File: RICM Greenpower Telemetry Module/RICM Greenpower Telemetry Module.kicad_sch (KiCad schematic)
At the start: 56 parts, among them J1 Jack-DC, J10 Conn_01x02_Female, J11 Conn_01x02_Female, J2 Conn_01x04_Female, J3 Conn_01x05_Female, J4 Conn_01x03_Female, J5 Conn_01x03_Female, J6 Conn_01x02_Female, J7 Conn_01x02_Female, J8 Conn_01x02_Female, J9 Conn_01x04_Female, U1 XL2001E1, U2 MT92165, U3 Pico, U4 Adafruit_MicroSD_SPI_SDIO, U5 ADS7830, U6 MPU_6050_module

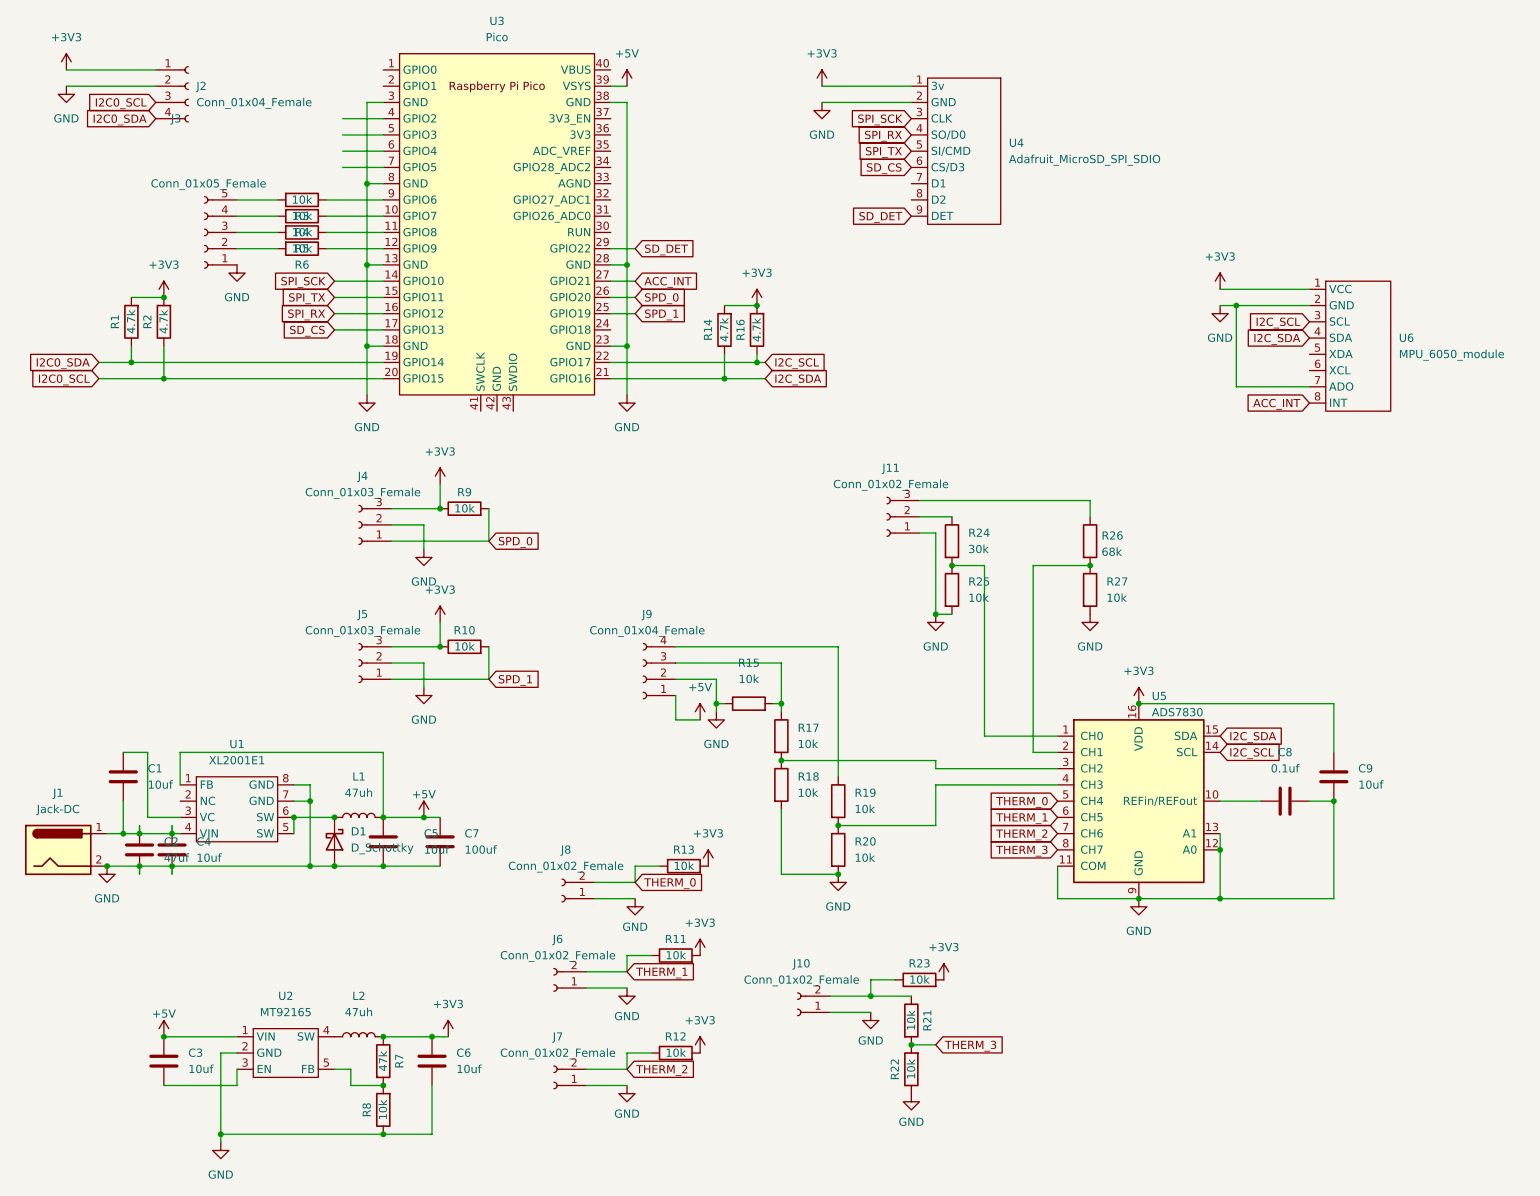
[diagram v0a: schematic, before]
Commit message: fixed errors discovered in v1 board
Connected vref on the ADS7830 to 3v3.
Corrected swapped pins on MT9216.
Added silkscreens and readjusted connector numbering.
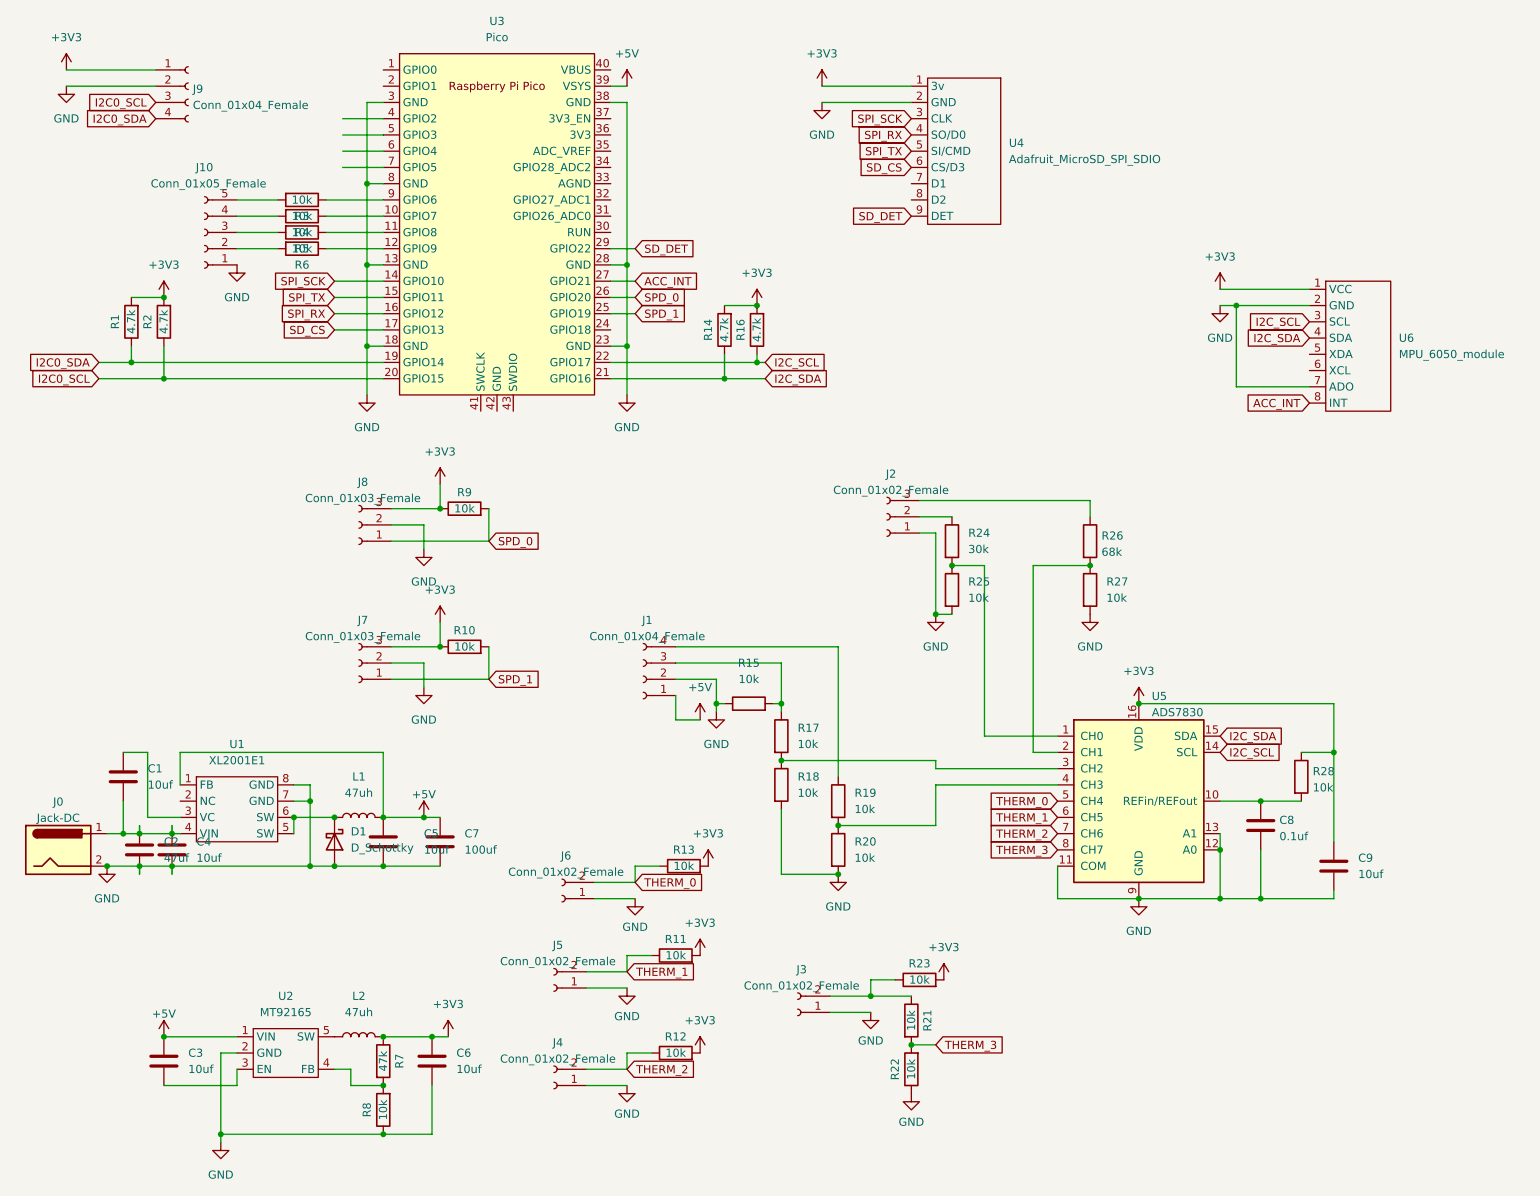
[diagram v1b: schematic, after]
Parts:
- added R28: 10k, Resistor_SMD:R_1206_3216Metric, symbol Device:R
- renumbered J1 to J0, J9 to J1, J3 to J10, J11 to J2, J10 to J3, J7 to J4, J6 to J5, J8 to J6, J5 to J7, J4 to J8, J2 to J9
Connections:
- net +3V3: now also R28.1
- net GND: now also C8.1; no longer C8.2
- net at R7.2, R8.2: now also U2.4 (FB); no longer U2.5 (FB)
- net at U5.10 (REFin/REFout): now also C8.2, R28.2; no longer C8.1
- net at L2.1: now also U2.5 (SW); no longer U2.4 (SW)
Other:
- moved on the sheet: C8, C9

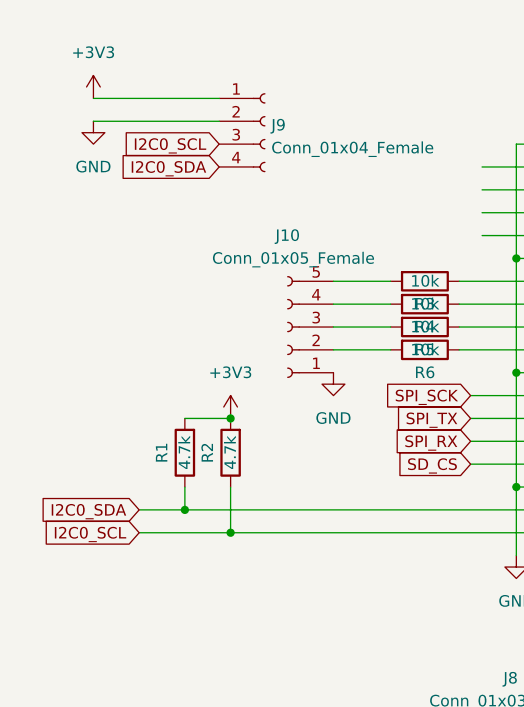
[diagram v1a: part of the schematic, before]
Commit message: added diags, bugfixes
Added libraries and associated diagnostics for OLED screens and GPIO buttons.
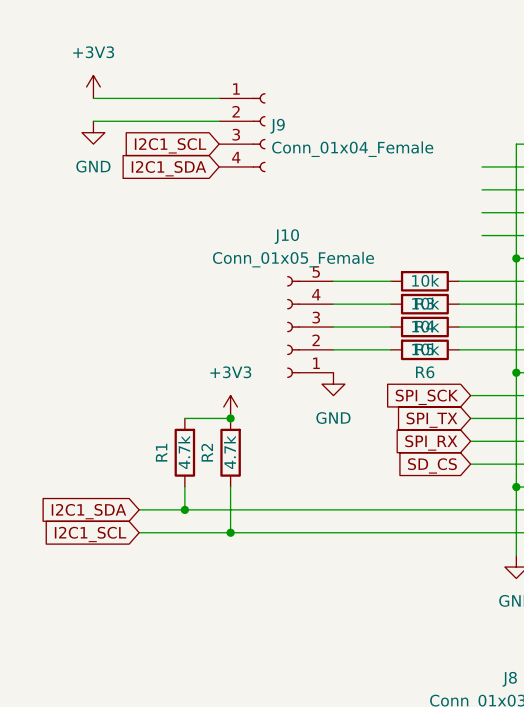
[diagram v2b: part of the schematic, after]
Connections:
- net I2C0_SCL renamed I2C1_SCL
- net I2C0_SDA renamed I2C1_SDA
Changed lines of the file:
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@@
     )
   )
-  (global_label "I2C0_SDA" (shape input) (at 34.29 30.48 180) (fields_autoplaced)
+  (global_label "I2C1_SDA" (shape input) (at 34.29 30.48 180) (fields_autoplaced)
     (effects (font (size 1.27 1.27)) (justify right))
-    (property "Intersheet References" "${INTERSHEET_REFS}" (id 0) (at 23.0474 30.5594 0)
+    (property "Intersheet References" "${INTERSHEET_REFS}" (id 0) (at 23.0474 30.4006 0)
       (effects (font (size 1.27 1.27)) (justify right) hide)
     )
@@
     )
   )
-  (global_label "I2C0_SCL" (shape input) (at 25.4 71.12 180) (fields_autoplaced)
+  (global_label "I2C1_SCL" (shape input) (at 25.4 71.12 180) (fields_autoplaced)
     (effects (font (size 1.27 1.27)) (justify right))
-    (property "Intersheet References" "${INTERSHEET_REFS}" (id 0) (at 14.2179 71.1994 0)
+    (property "Intersheet References" "${INTERSHEET_REFS}" (id 0) (at 14.2179 71.0406 0)
       (effects (font (size 1.27 1.27)) (justify right) hide)
     )
@@
     )
   )
-  (global_label "I2C0_SCL" (shape input) (at 34.29 27.94 180) (fields_autoplaced)
+  (global_label "I2C1_SCL" (shape input) (at 34.29 27.94 180) (fields_autoplaced)
     (effects (font (size 1.27 1.27)) (justify right))
-    (property "Intersheet References" "${INTERSHEET_REFS}" (id 0) (at 23.1079 28.0194 0)
+    (property "Intersheet References" "${INTERSHEET_REFS}" (id 0) (at 23.1079 27.8606 0)
       (effects (font (size 1.27 1.27)) (justify right) hide)
     )
@@
     )
   )
-  (global_label "I2C0_SDA" (shape input) (at 25.4 68.58 180) (fields_autoplaced)
+  (global_label "I2C1_SDA" (shape input) (at 25.4 68.58 180) (fields_autoplaced)
     (effects (font (size 1.27 1.27)) (justify right))
-    (property "Intersheet References" "${INTERSHEET_REFS}" (id 0) (at 14.1574 68.6594 0)
+    (property "Intersheet References" "${INTERSHEET_REFS}" (id 0) (at 14.1574 68.5006 0)
       (effects (font (size 1.27 1.27)) (justify right) hide)
     )

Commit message: Fixed footprints and silkscreen
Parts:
- C2: footprint Capacitor_THT:CP_Radial_D8.0mm_P3.50mm -> Capacitor_THT:CP_Radial_D5.0mm_P2.00mm
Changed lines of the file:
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@@
       (effects (font (size 1.27 1.27)) (justify left))
     )
-    (property "Footprint" "Capacitor_THT:CP_Radial_D8.0mm_P3.50mm" (id 2) (at 32.7152 148.59 0)
+    (property "Footprint" "Capacitor_THT:CP_Radial_D5.0mm_P2.00mm" (id 2) (at 32.7152 148.59 0)
       (effects (font (size 1.27 1.27)) hide)
     )
@@
     )
     (path "/0d18f623-67ed-4824-a618-f2eb436b25c6"
-      (reference "C2") (unit 1) (value "47uf") (footprint "Capacitor_THT:CP_Radial_D8.0mm_P3.50mm")
+      (reference "C2") (unit 1) (value "47uf") (footprint "Capacitor_THT:CP_Radial_D5.0mm_P2.00mm")
     )
     (path "/71b5cd3e-ae0b-4068-9f4c-5ceaa9425277"

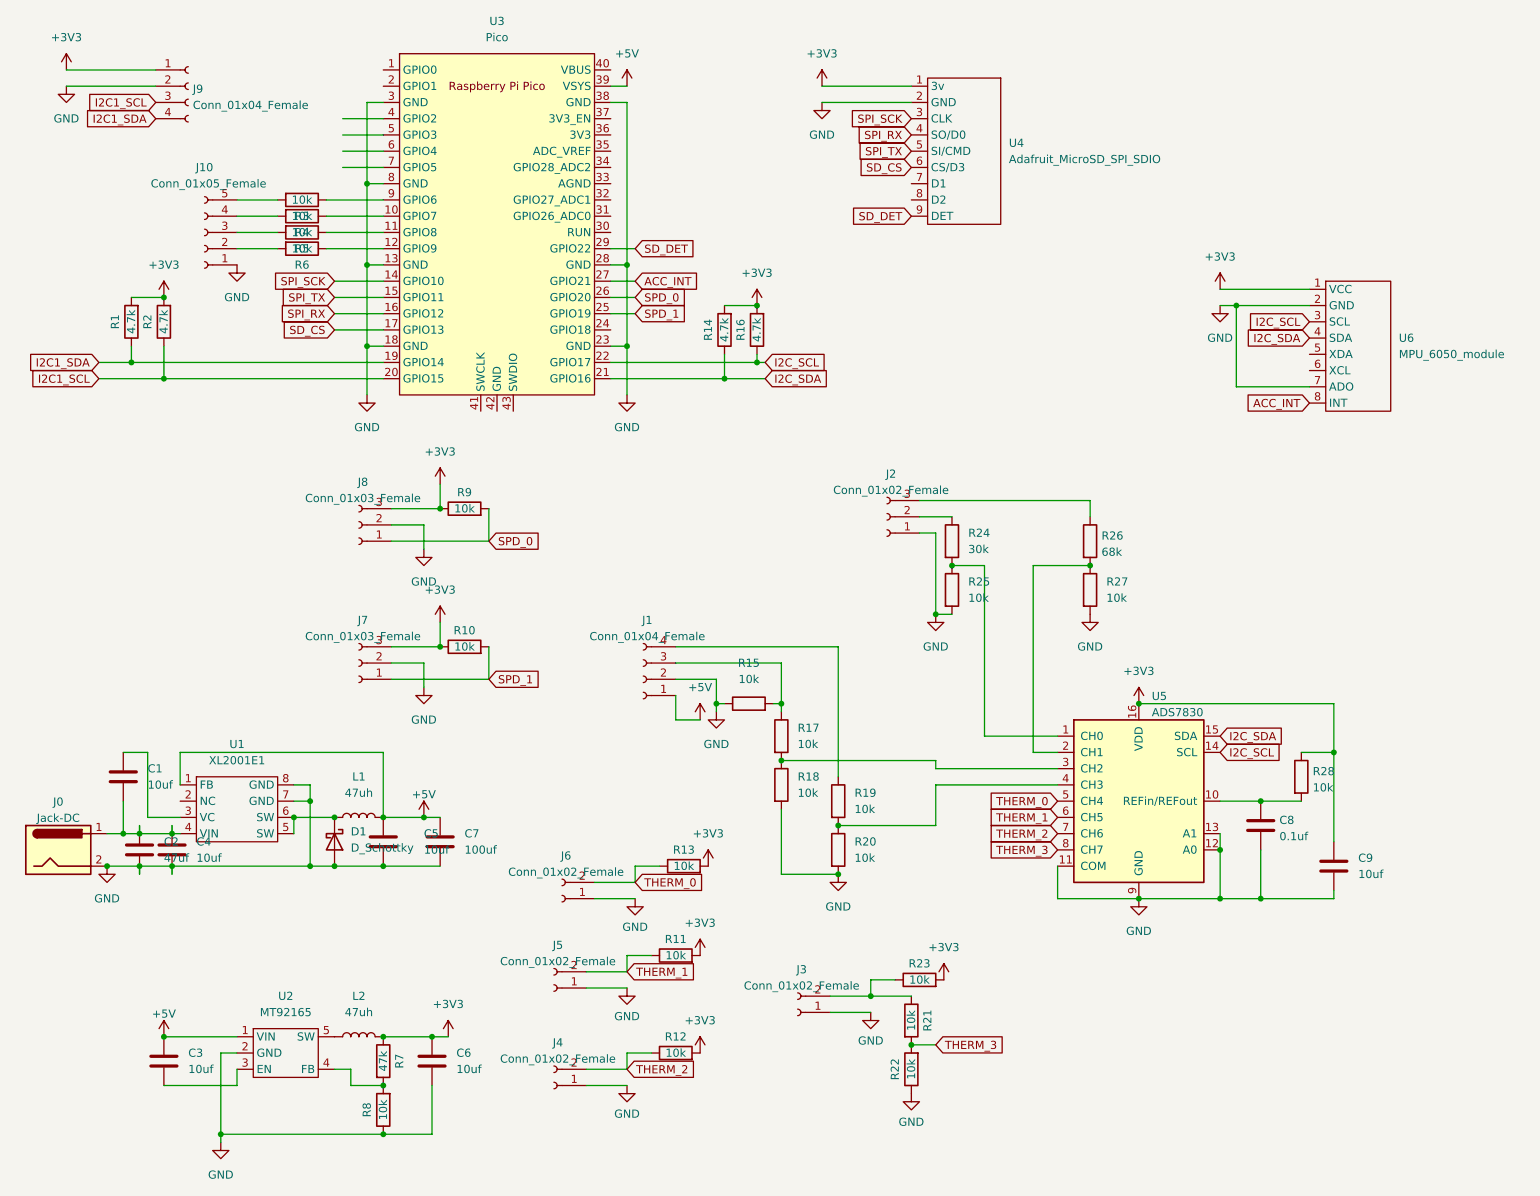
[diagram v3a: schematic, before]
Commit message: Schematic and layout corrections
Added revision silkscreen to schematic. Fixed pinout of display connector to match standard i2c pinout. Added schematic notes explaining resistor options for THERM_3.
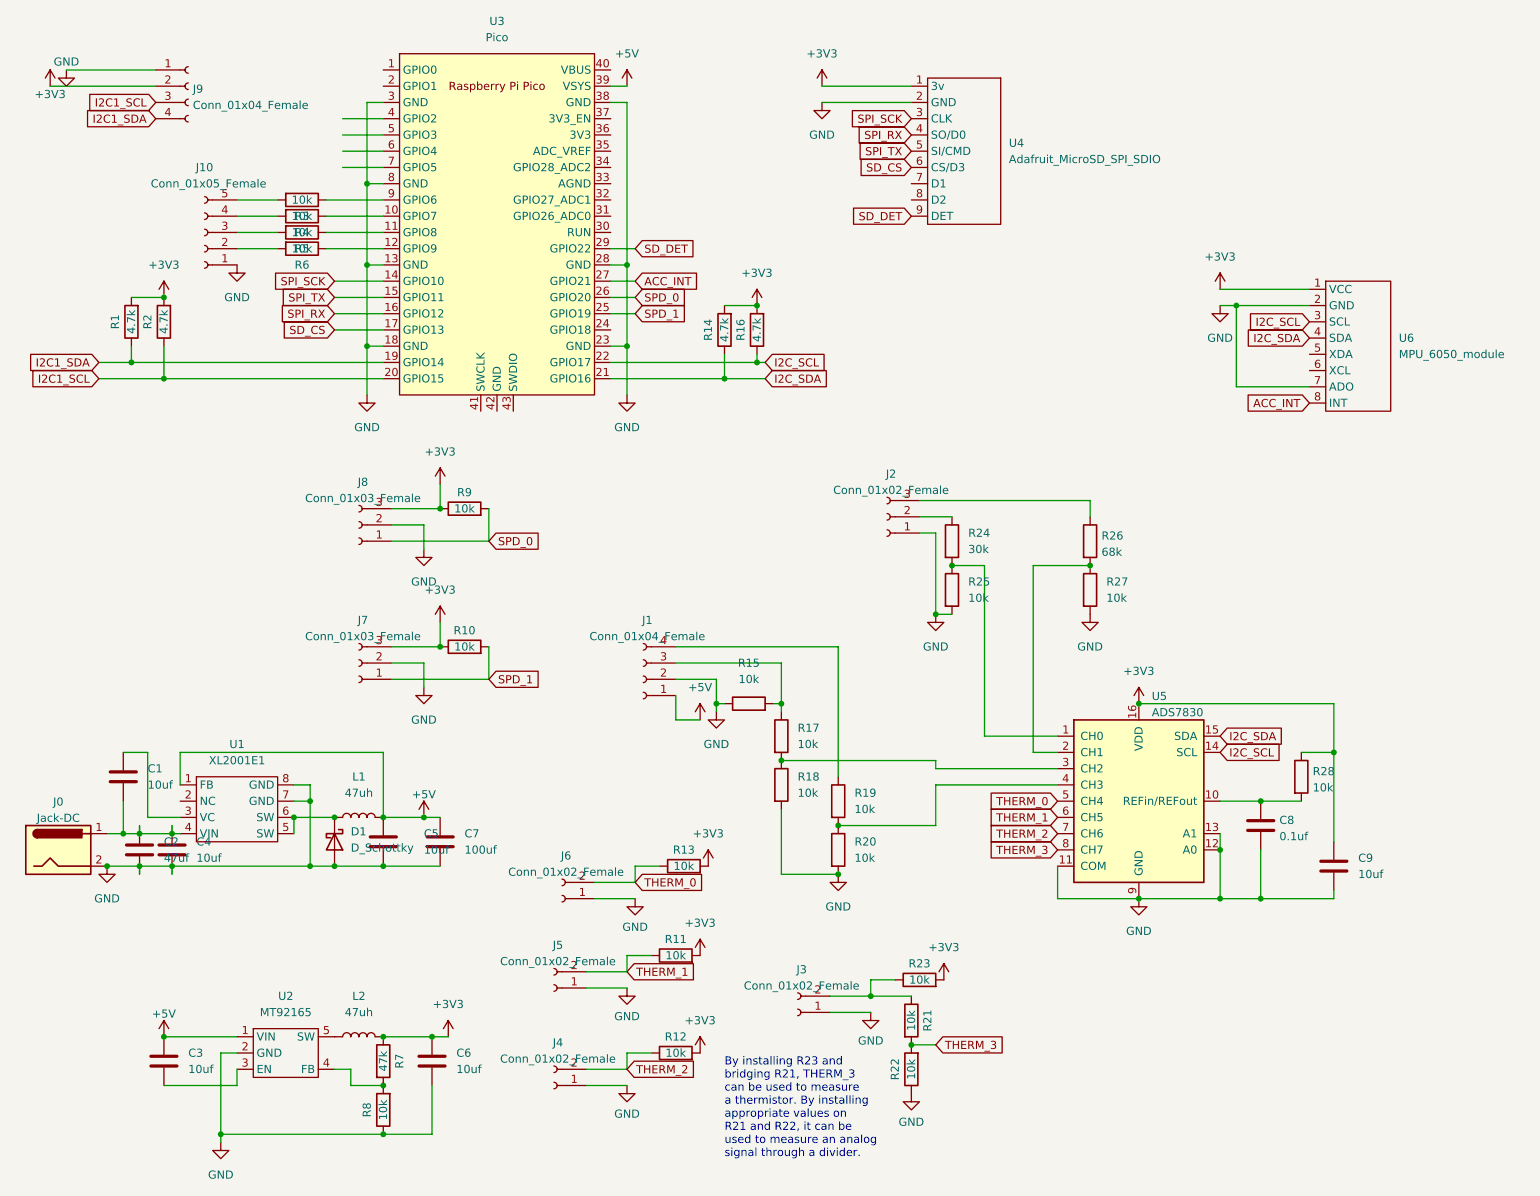
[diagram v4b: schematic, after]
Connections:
- net +3V3: now also J9.2 (Pin_2); no longer J9.1 (Pin_1)
- net GND: now also J9.1 (Pin_1); no longer J9.2 (Pin_2)
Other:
- note added: "By installing R23 and bridging R21, THERM_3 can be used to measure a thermistor. By installing appropriate values on R21 and R22, it can be used to measure an analog signal through a divider."
